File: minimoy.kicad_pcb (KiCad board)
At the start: 2 copper layers, 33 parts, among them J1 Barrel_Jack, J2 Conn_02x02_Odd_Even, J3 Conn_02x02_Odd_Even, J4 Conn_02x02_Odd_Even, J5 AudioJack3_Ground, J6 Conn_02x02_Odd_Even, J7 AudioJack3_Ground, SW1 Rotary_Encoder, U1 MAX5440EAG, U2 TLE2426xD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

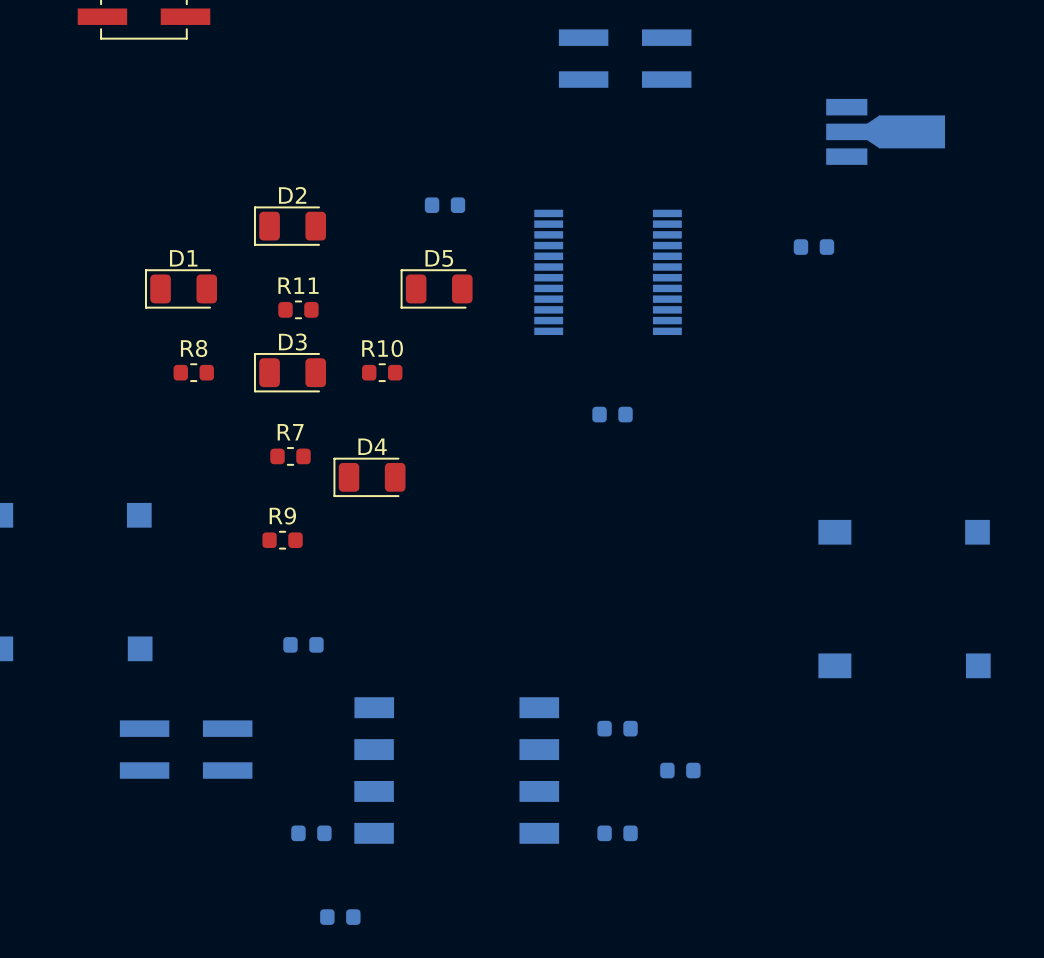
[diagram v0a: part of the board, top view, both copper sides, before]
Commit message: Placed upper board.
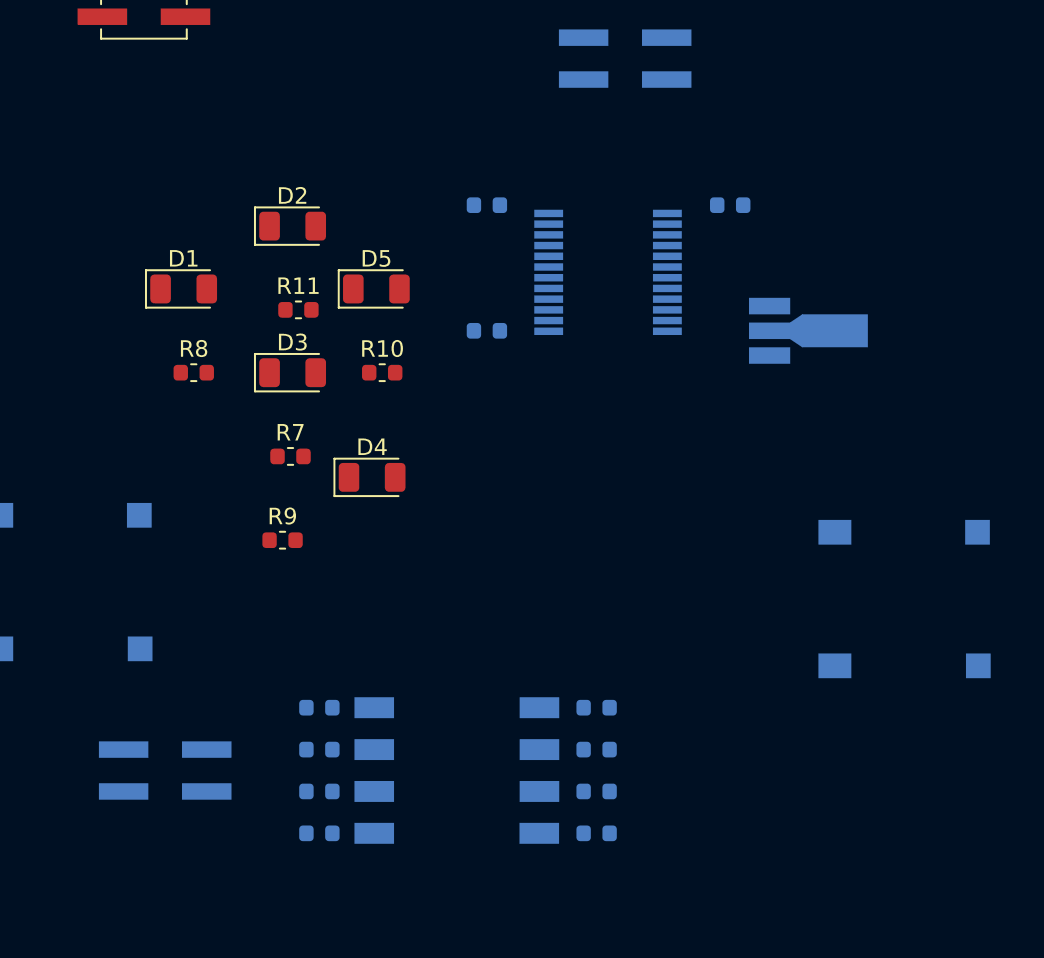
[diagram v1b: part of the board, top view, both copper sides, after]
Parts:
- added R1: 10k, Resistor_SMD:R_0603_1608Metric, B.Cu at (25.9, 108.0)
- added R2: 10k, Resistor_SMD:R_0603_1608Metric, B.Cu at (42.7, 105.4)
- moved R4 22.2 mm to (25.9, 113.0)
- moved C5 21.1 mm to (42.7, 113.0)
- moved C6 19.6 mm to (25.9, 105.4)
- moved R5 18.6 mm to (42.7, 108.0)
- moved R6 18.5 mm to (25.9, 110.5)
- moved R3 17.5 mm to (42.7, 110.5)
- moved C1 14.8 mm to (36.0, 74.9), turned to 180 degrees
- moved U4 12.9 mm to (55.2, 82.5)
- moved C3 8.03 mm to (36.0, 82.5), turned to 180 degrees
- moved C7 5.68 mm to (50.8, 74.9), turned to 180 degrees
- moved D5 3.81 mm to (29.3, 80.0)
- moved J6 1.80 mm to (16.5, 109.2)
- turned U3 to 180 degrees
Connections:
- J5 pad T: /-12V_UPPER -> Net-(J5-PadT)
- R5 pad 1: /-12V_UPPER -> Net-(R2-Pad2)
- R6 pad 1: Net-(J5-PadR) -> Net-(R1-Pad2)
- U3 pad 1: /-12V_UPPER -> Net-(J5-PadT)
- U3 pad 2: /-12V_UPPER -> Net-(R2-Pad2)
- U3 pad 6: Net-(J5-PadR) -> Net-(R1-Pad2)

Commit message: Larger PCB.
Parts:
- removed C1, C3, C7: 0.1uF, Capacitor_SMD:C_0603_1608Metric
- removed C5, C6: 0.22uF, Capacitor_SMD:C_0603_1608Metric
- removed D1, D2, D3, D4, D5: LED, LED_SMD:LED_1206_3216Metric
- removed J2, J6: Conn_02x02_Odd_Even, Connector_PinSocket_2.54mm:PinSocket_2x02_P2.54mm_Vertical_SMD
- removed J5, J7: AudioJack3_Ground, footprints:STEREO_JACK_SMD
- removed R1, R2: 10k, Resistor_SMD:R_0603_1608Metric
- removed R10, R11, R7, R8, R9: 680, Resistor_SMD:R_0603_1608Metric
- removed R3, R4: 100k, Resistor_SMD:R_0603_1608Metric
- removed R5, R6: 1k, Resistor_SMD:R_0603_1608Metric
- removed U1: MAX5440EAG, Package_SO:SSOP-24_5.3x8.2mm_P0.65mm
- removed U3: OPA2134, footprints:DIL_8_SMD
- U4: moved to F.Cu
- moved J3 101.6 mm to (113.0, 90.0), turned to 270 degrees
- moved J1 84.5 mm to (100.0, 84.0)
- moved SW1 81.3 mm to (100.0, 100.0)
- moved U2 75.6 mm to (114.5, 104.8)
- moved J4 64.9 mm to (86.0, 110.0), turned to 270 degrees
- moved U4 63.7 mm to (111.0, 113.3), turned to 270 degrees
- moved C4 63.6 mm to (114.5, 99.7), turned to 180 degrees
- moved C2 61.4 mm to (88.0, 88.0), turned to 270 degrees
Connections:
- J3 pad 2: GND -> /VGND_LOWER
- J3 pad 4: GND -> /VGND_LOWER
- J4 pad 1: /VGND_LOWER -> Net-(J4-Pad1)
- U4 pad 1: /+12V_UPPER -> +24V
- U4 pad 2: /VGND_UPPER -> /VGND_LOWER
- U4 pad 3: /+5V_UPPER -> Net-(J4-Pad1)
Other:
- board outline added: 44 x 44 mm
